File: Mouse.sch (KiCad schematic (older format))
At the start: 31 parts, among them J1 Conn_01x05_Male, U1 Left click, U2 Middle click, U3 Right Click, U4 LQ1, U5 Optical_Sensor

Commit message: Layout Updated
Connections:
- net Pin_2: no longer U1.2 (NO), U4.2
- net at LD2.1 (K): now also JP3.1; no longer R12.2
- net at LD2.2 (A): now also R12.2; no longer JP3.1
- net Pin_2J: now reaches C16.1, JP1.1, LD1.2 (A)
- net Pin_2J: now also U1.2 (NO), U4.2
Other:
- moved on the sheet: JP1, LD2, R12, U4
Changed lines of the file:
@@
 	4200 2650 4100 2650
 Text GLabel 2350 1550 0    50   Input ~ 0
-Pin_2
+Pin_2J
 Wire Wire Line
 	1300 4700 1100 4700
@@
 $EndComp
 $Comp
-L Device:C C8
-U 1 1 62FC41C4
-P 6300 2250
-F 0 "C8" V 6552 2250 50  0000 C CNN
-F 1 "C" V 6461 2250 50  0000 C CNN
-F 2 "Mouse:R_0603_1608_Logi" H 6338 2100 50  0001 C CNN
-F 3 "~" H 6300 2250 50  0001 C CNN
-	1    6300 2250
-	0    -1   -1   0
-$EndComp
-$Comp
 L power:GNDREF #PWR0109
 U 1 1 62FC9AD8
@@
 Wire Wire Line
 	6150 2250 5850 2250
-Text GLabel 6150 2400 0    50   Input ~ 0
-D-
 Wire Notes Line
 	550  7250 2850 7250
@@
 Text GLabel 5850 2250 0    50   Input ~ 0
 Pin_8
-Wire Wire Line
-	6200 2250 6200 2400
-Wire Wire Line
-	6200 2400 6150 2400
 Text GLabel 2700 3350 2    50   Input ~ 0
 Pin_7
@@
 Text GLabel 1550 6400 0    50   Input ~ 0
 Pin_3
-Text GLabel 850  6350 0    50   Input ~ 0
+Text GLabel 900  6350 0    50   Input ~ 0
 Pin_4
 $Comp
 L power:GNDREF #PWR0112
 U 1 1 62F9DBF5
-P 850 6550
-F 0 "#PWR0112" H 850 6300 50  0001 C CNN
-F 1 "GNDREF" V 855 6422 50  0000 R CNN
-F 2 "" H 850 6550 50  0001 C CNN
-F 3 "" H 850 6550 50  0001 C CNN
-	1    850  6550
-	1    0    0    -1
-$EndComp
-Text GLabel 850  6450 0    50   Input ~ 0
-Pin_2
+P 900 6550
+F 0 "#PWR0112" H 900 6300 50  0001 C CNN
+F 1 "GNDREF" V 905 6422 50  0000 R CNN
+F 2 "" H 900 6550 50  0001 C CNN
+F 3 "" H 900 6550 50  0001 C CNN
+	1    900  6550
+	1    0    0    -1
+$EndComp
+Text GLabel 900  6450 0    50   Input ~ 0
+Pin_2J
 $Comp
 L Optical_Mouse:LQ U4
 U 1 1 62F9C524
-P 1000 6350
-F 0 "U4" H 1078 6311 50  0000 L CNN
-F 1 "LQ1" H 1078 6220 50  0000 L CNN
-F 2 "Mouse:LQ1" H 1000 6450 50  0001 C CNN
-F 3 "" H 1000 6450 50  0001 C CNN
-	1    1000 6350
-	1    0    0    -1
-$EndComp
-Text GLabel 2550 6700 3    50   Input ~ 0
-Pin_2
+P 1050 6350
+F 0 "U4" H 1128 6311 50  0000 L CNN
+F 1 "LQ1" H 1128 6220 50  0000 L CNN
+F 2 "Mouse:LQ1" H 1050 6450 50  0001 C CNN
+F 3 "" H 1050 6450 50  0001 C CNN
+	1    1050 6350
+	1    0    0    -1
+$EndComp
 $Comp
 L LED:LD271 LD1
@@
 Wire Notes Line
 	550  4300 3250 4300
-Text GLabel 4950 1000 2    50   Input ~ 0
-Pin_1
 $Comp
 L Device:R R12
 U 1 1 62F83C24
-P 4200 1000
-F 0 "R12" V 3993 1000 50  0000 C CNN
-F 1 "330 LD2 resistor" V 4084 1000 50  0000 C CNN
-F 2 "Mouse:R_0603_1608_Logi" V 4130 1000 50  0001 C CNN
-F 3 "~" H 4200 1000 50  0001 C CNN
-	1    4200 1000
-	0    -1   -1   0
-$EndComp
-$Comp
-L LED:LD271 LD2
-U 1 1 62F8164E
-P 4550 1000
-F 0 "LD2" H 4500 1290 50  0000 C CNN
-F 1 "Sensor illumination" H 4500 1199 50  0000 C CNN
-F 2 "Mouse:LED_Sensor" H 4550 1175 50  0001 C CNN
-F 3 "http://www.alliedelec.com/m/d/40788c34903a719969df15f1fbea1056.pdf" H 4500 1000 50  0001 C CNN
-	1    4550 1000
-	1    0    0    -1
+P 3950 1000
+F 0 "R12" V 3743 1000 50  0000 C CNN
+F 1 "330 LD2 resistor" V 3834 1000 50  0000 C CNN
+F 2 "Mouse:R_0603_1608_Logi" V 3880 1000 50  0001 C CNN
+F 3 "~" H 3950 1000 50  0001 C CNN
+	1    3950 1000
+	0    -1   -1   0
 $EndComp
 Connection ~ 4200 2650
@@
 NoConn ~ 1000 2400
 $Comp
-L Device:R JP1
-U 1 1 63EBDACF
-P 2550 6550
-F 0 "JP1" H 2620 6596 50  0000 L CNN
-F 1 "R" H 2620 6505 50  0000 L CNN
-F 2 "Mouse:JP_Axial_DIN0207_L6.3mm_D2.5mm_P10.16mm_Horizontal" V 2480 6550 50  0001 C CNN
-F 3 "~" H 2550 6550 50  0001 C CNN
-	1    2550 6550
-	1    0    0    -1
-$EndComp
-$Comp
 L Device:R JP2
 U 1 1 63EBE5D2
@@
 	1    0    0    -1
 $EndComp
-Text GLabel 4050 1000 0    50   Input ~ 0
+Text GLabel 3800 1000 0    50   Input ~ 0
 Pin_5
+$Comp
+L power:GNDREF #PWR0104
+U 1 1 62FA90BC
+P 6400 1600
+F 0 "#PWR0104" H 6400 1350 50  0001 C CNN
+F 1 "GNDREF" H 6593 1457 50  0000 R CNN
+F 2 "" H 6400 1600 50  0001 C CNN
+F 3 "" H 6400 1600 50  0001 C CNN
+	1    6400 1600
+	1    0    0    -1
+$EndComp
+Wire Notes Line
+	6950 600  3450 600
+$Comp
+L Device:R R16
+U 1 1 62F9F594
+P 5850 1000
+F 0 "R16" V 6057 1000 50  0000 C CNN
+F 1 "R 000" V 5966 1000 50  0000 C CNN
+F 2 "Mouse:R_0603_1608_Logi" V 5780 1000 50  0001 C CNN
+F 3 "~" H 5850 1000 50  0001 C CNN
+	1    5850 1000
+	0    -1   -1   0
+$EndComp
+Connection ~ 6000 1000
+Wire Wire Line
+	5700 1000 5700 1150
+Wire Wire Line
+	1800 2400 1700 2400
+$Comp
+L Device:C C8
+U 1 1 62FC41C4
+P 6300 2250
+F 0 "C8" V 6552 2250 50  0000 C CNN
+F 1 "C" V 6461 2250 50  0000 C CNN
+F 2 "Mouse:R_0603_1608_Logi" H 6338 2100 50  0001 C CNN
+F 3 "~" H 6300 2250 50  0001 C CNN
+	1    6300 2250
+	0    -1   -1   0
+$EndComp
+Text GLabel 2600 6800 3    50   Input ~ 0
+Pin_2
+$Comp
+L Device:R JP1
+U 1 1 63EBDACF
+P 2600 6650
+F 0 "JP1" H 2670 6696 50  0000 L CNN
+F 1 "R" H 2670 6605 50  0000 L CNN
+F 2 "Mouse:JP_Axial_DIN0207_L6.3mm_D2.5mm_P10.16mm_Horizontal" V 2530 6650 50  0001 C CNN
+F 3 "~" H 2600 6650 50  0001 C CNN
+	1    2600 6650
+	1    0    0    -1
+$EndComp
+Wire Wire Line
+	6200 2250 6200 2400
+Wire Wire Line
+	6200 2400 6150 2400
+Text GLabel 6150 2400 0    50   Input ~ 0
+D-
 $Comp
 L Device:R JP3
@@
 $EndComp
 $Comp
-L power:GNDREF #PWR0104
-U 1 1 62FA90BC
-P 6400 1600
-F 0 "#PWR0104" H 6400 1350 50  0001 C CNN
-F 1 "GNDREF" H 6593 1457 50  0000 R CNN
-F 2 "" H 6400 1600 50  0001 C CNN
-F 3 "" H 6400 1600 50  0001 C CNN
-	1    6400 1600
-	1    0    0    -1
-$EndComp
-Wire Wire Line
-	2150 6400 2550 6400
+L LED:LD271 LD2
+U 1 1 62F8164E
+P 4450 1000
+F 0 "LD2" H 4400 1290 50  0000 C CNN
+F 1 "Sensor illumination" H 4400 1199 50  0000 C CNN
+F 2 "Mouse:LED_Sensor" H 4450 1175 50  0001 C CNN
+F 3 "http://www.alliedelec.com/m/d/40788c34903a719969df15f1fbea1056.pdf" H 4400 1000 50  0001 C CNN
+	1    4450 1000
+	-1   0    0    1
+$EndComp
+Text GLabel 4950 1000 2    50   Input ~ 0
+Pin_1
+Wire Wire Line
+	4350 1000 4100 1000
+Text GLabel 2600 6400 1    50   Input ~ 0
+Pin_2J
+Wire Wire Line
+	2150 6400 2600 6400
 Connection ~ 2150 6400
-Wire Notes Line
-	6950 600  3450 600
-$Comp
-L Device:R R16
-U 1 1 62F9F594
-P 5850 1000
-F 0 "R16" V 6057 1000 50  0000 C CNN
-F 1 "R 000" V 5966 1000 50  0000 C CNN
-F 2 "Mouse:R_0603_1608_Logi" V 5780 1000 50  0001 C CNN
-F 3 "~" H 5850 1000 50  0001 C CNN
-	1    5850 1000
-	0    -1   -1   0
-$EndComp
-Connection ~ 6000 1000
-Wire Wire Line
-	5700 1000 5700 1150
-Wire Wire Line
-	1800 2400 1700 2400
+Wire Wire Line
+	2600 6500 2600 6400
 $EndSCHEMATC

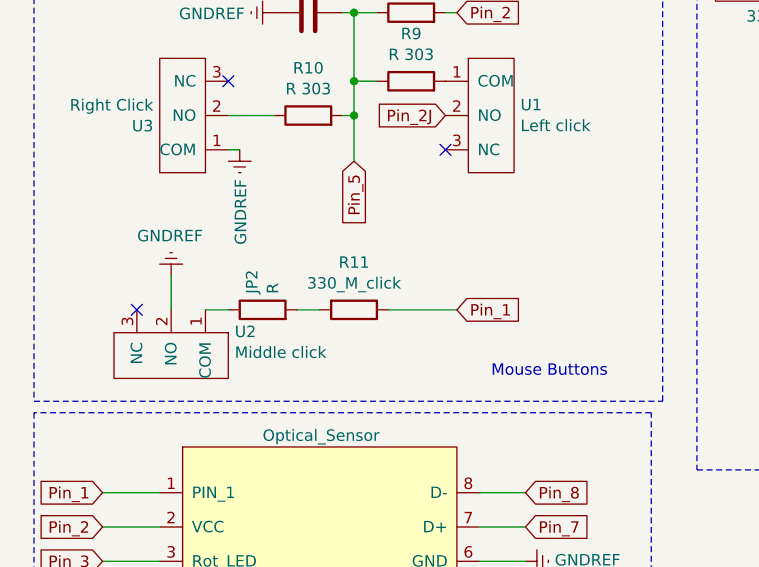
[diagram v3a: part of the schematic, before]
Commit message: Updated Schematics, Layout and Footprints
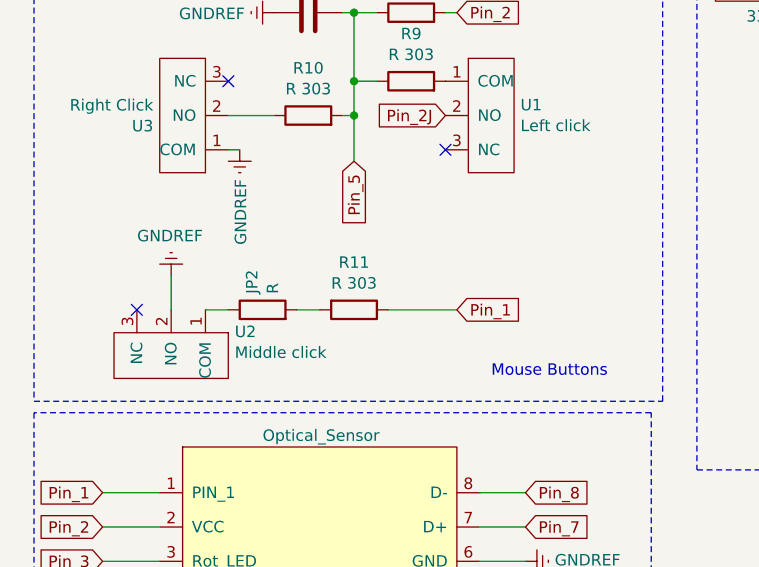
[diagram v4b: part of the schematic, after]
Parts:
- R11: value 330_M_click -> R 303
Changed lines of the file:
@@
 P 1950 2400
 F 0 "R11" V 1743 2400 50  0000 C CNN
-F 1 "330_M_click" V 1834 2400 50  0000 C CNN
+F 1 "R 303" V 1834 2400 50  0000 C CNN
 F 2 "Mouse:R_0603_1608_Logi" V 1880 2400 50  0001 C CNN
 F 3 "~" H 1950 2400 50  0001 C CNN

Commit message: Schematic Correction
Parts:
- C11, C13: value C -> C NC
- C12, C15: value C -> C 0.1uF
- C14: value C -> C 4.7uF
- C8, C9: value C -> C 0.01uF
- LQ1: renamed from U4; value LQ1 -> EL
- R12: value 330 LD2 resistor -> R 330
- R17: value R -> R NC
- renumbered U1 to SW1, U3 to SW2, U2 to SW3, U5 to U1
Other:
- moved on the sheet: C14, C15, JP4, R15, R16
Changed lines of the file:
@@
 $EndDescr
 $Comp
-L Optical_Mouse:switch U1
+L Optical_Mouse:switch SW1
 U 1 1 62F7695E
 P 2550 1550
-F 0 "U1" H 2678 1596 50  0000 L CNN
+F 0 "SW1" H 2678 1596 50  0000 L CNN
 F 1 "Left click" H 2678 1505 50  0000 L CNN
 F 2 "Mouse:SPDT_Switch" H 2800 1650 50  0001 C CNN
@@
 P 4350 2200
 F 0 "R17" V 4557 2200 50  0000 C CNN
-F 1 "R" V 4466 2200 50  0000 C CNN
+F 1 "R NC" V 4466 2200 50  0000 C CNN
 F 2 "Mouse:R_0603_1608_Logi" V 4280 2200 50  0001 C CNN
 F 3 "~" H 4350 2200 50  0001 C CNN
@@
 P 4650 2200
 F 0 "C13" V 4902 2200 50  0000 C CNN
-F 1 "C" V 4811 2200 50  0000 C CNN
+F 1 "C NC" V 4811 2200 50  0000 C CNN
 F 2 "Mouse:R_0603_1608_Logi" H 4688 2050 50  0001 C CNN
 F 3 "~" H 4650 2200 50  0001 C CNN
@@
 	1300 4600 1450 4600
 $Comp
-L Device:R R15
-U 1 1 62F9F9E0
-P 6150 1000
-F 0 "R15" V 6357 1000 50  0000 C CNN
-F 1 "R 1R0" V 6266 1000 50  0000 C CNN
-F 2 "Mouse:R_0603_1608_Logi" V 6080 1000 50  0001 C CNN
-F 3 "~" H 6150 1000 50  0001 C CNN
-	1    6150 1000
-	0    -1   -1   0
-$EndComp
-$Comp
 L Device:R R13
 U 1 1 62F9FE60
@@
 	0    -1   -1   0
 $EndComp
-$Comp
-L Device:C C14
-U 1 1 62FA0303
-P 6000 1450
-F 0 "C14" H 5885 1404 50  0000 R CNN
-F 1 "C" H 5885 1495 50  0000 R CNN
-F 2 "Mouse:R_0603_1608_Logi" H 6038 1300 50  0001 C CNN
-F 3 "~" H 6000 1450 50  0001 C CNN
-	1    6000 1450
-	-1   0    0    1
-$EndComp
-$Comp
-L Device:C C15
-U 1 1 62FA0A45
-P 6400 1450
-F 0 "C15" H 6515 1496 50  0000 L CNN
-F 1 "C" H 6515 1405 50  0000 L CNN
-F 2 "Mouse:R_0603_1608_Logi" H 6438 1300 50  0001 C CNN
-F 3 "~" H 6400 1450 50  0001 C CNN
-	1    6400 1450
-	1    0    0    -1
-$EndComp
-Text GLabel 5700 1450 3    50   Input ~ 0
-Pin_2
-Wire Wire Line
-	6000 1000 6000 1200
-Connection ~ 6000 1200
-Wire Wire Line
-	6000 1200 6000 1300
-Wire Wire Line
-	6400 1300 6400 1200
-Wire Wire Line
-	6000 1200 6400 1200
 Text GLabel 1100 4800 2    50   Input ~ 0
 VCC
@@
 Text GLabel 1300 5400 3    50   Input ~ 0
 D-
-Text GLabel 6450 1000 2    50   Input ~ 0
-VCC
-Wire Wire Line
-	6450 1000 6300 1000
-$Comp
-L power:GNDREF #PWR0103
-U 1 1 62FA8905
-P 6000 1600
-F 0 "#PWR0103" H 6000 1350 50  0001 C CNN
-F 1 "GNDREF" H 6199 1457 50  0000 R CNN
-F 2 "" H 6000 1600 50  0001 C CNN
-F 3 "" H 6000 1600 50  0001 C CNN
-	1    6000 1600
-	1    0    0    -1
-$EndComp
 Text GLabel 850  3650 0    50   Input ~ 0
 Pin_4
@@
 P 1750 1100
 F 0 "C11" V 2002 1100 50  0000 C CNN
-F 1 "C" V 1911 1100 50  0000 C CNN
+F 1 "C NC" V 1911 1100 50  0000 C CNN
 F 2 "Mouse:R_0603_1608_Logi" H 1788 950 50  0001 C CNN
 F 3 "~" H 1750 1100 50  0001 C CNN
@@
 P 4650 1650
 F 0 "C9" V 4902 1650 50  0000 C CNN
-F 1 "C" V 4811 1650 50  0000 C CNN
+F 1 "C  0.01uF" V 4811 1650 50  0000 C CNN
 F 2 "Mouse:R_0603_1608_Logi" H 4688 1500 50  0001 C CNN
 F 3 "~" H 4650 1650 50  0001 C CNN
@@
 	550  7250 2850 7250
 $Comp
-L Optical_Mouse:switch U3
+L Optical_Mouse:switch SW2
 U 1 1 62F77846
 P 1200 1550
-F 0 "U3" H 1328 1596 50  0000 L CNN
+F 0 "SW2" H 1328 1596 50  0000 L CNN
 F 1 "Right Click" H 1328 1505 50  0000 L CNN
 F 2 "Mouse:SPDT_Switch" H 1450 1650 50  0001 C CNN
@@
 $EndComp
 $Comp
-L Optical_Mouse:switch U2
+L Optical_Mouse:switch SW3
 U 1 1 62F76FC9
 P 1150 2600
-F 0 "U2" V 1046 2878 50  0000 L CNN
+F 0 "SW3" V 1046 2878 50  0000 L CNN
 F 1 "Middle click" V 1137 2878 50  0000 L CNN
 F 2 "Mouse:SPDT_Switch" H 1400 2700 50  0001 C CNN
@@
 Pin_2J
 $Comp
-L Optical_Mouse:LQ U4
+L Optical_Mouse:LQ LQ1
 U 1 1 62F9C524
 P 1050 6350
-F 0 "U4" H 1128 6311 50  0000 L CNN
-F 1 "LQ1" H 1128 6220 50  0000 L CNN
+F 0 "LQ1" H 1128 6311 50  0000 L CNN
+F 1 "EL" H 1128 6220 50  0000 L CNN
 F 2 "Mouse:LQ1" H 1050 6450 50  0001 C CNN
 F 3 "" H 1050 6450 50  0001 C CNN
@@
 P 3950 1000
 F 0 "R12" V 3743 1000 50  0000 C CNN
-F 1 "330 LD2 resistor" V 3834 1000 50  0000 C CNN
+F 1 "R 330 " V 3834 1000 50  0000 C CNN
 F 2 "Mouse:R_0603_1608_Logi" V 3880 1000 50  0001 C CNN
 F 3 "~" H 3950 1000 50  0001 C CNN
@@
 P 4650 2650
 F 0 "C12" V 4902 2650 50  0000 C CNN
-F 1 "C" V 4811 2650 50  0000 C CNN
+F 1 "C 0.1uF" V 4811 2650 50  0000 C CNN
 F 2 "Mouse:R_0603_1608_Logi" H 4688 2500 50  0001 C CNN
 F 3 "~" H 4650 2650 50  0001 C CNN
@@
 	2500 3650 2700 3650
 $Comp
-L Optical_Mouse:Optical_Sensor U5
+L Optical_Mouse:Optical_Sensor U1
 U 1 1 62F7519C
 P 1800 3450
-F 0 "U5" H 1750 3150 50  0000 L CNN
+F 0 "U1" H 1750 3150 50  0000 L CNN
 F 1 "Optical_Sensor" H 1550 3950 50  0000 L CNN
 F 2 "Mouse:Sensor" H 1800 3450 50  0001 C CNN
@@
 	0    -1   -1   0
 $EndComp
-$Comp
-L Device:R JP4
-U 1 1 63EBF40A
-P 5700 1300
-F 0 "JP4" H 5770 1346 50  0000 L CNN
-F 1 "R" H 5770 1255 50  0000 L CNN
-F 2 "Mouse:JP_Axial_DIN0207_L6.3mm_D2.5mm_P10.16mm_Horizontal" V 5630 1300 50  0001 C CNN
-F 3 "~" H 5700 1300 50  0001 C CNN
-	1    5700 1300
-	1    0    0    -1
-$EndComp
 Text GLabel 3800 1000 0    50   Input ~ 0
 Pin_5
-$Comp
-L power:GNDREF #PWR0104
-U 1 1 62FA90BC
-P 6400 1600
-F 0 "#PWR0104" H 6400 1350 50  0001 C CNN
-F 1 "GNDREF" H 6593 1457 50  0000 R CNN
-F 2 "" H 6400 1600 50  0001 C CNN
-F 3 "" H 6400 1600 50  0001 C CNN
-	1    6400 1600
-	1    0    0    -1
-$EndComp
-Wire Notes Line
-	6950 600  3450 600
-$Comp
-L Device:R R16
-U 1 1 62F9F594
-P 5850 1000
-F 0 "R16" V 6057 1000 50  0000 C CNN
-F 1 "R 000" V 5966 1000 50  0000 C CNN
-F 2 "Mouse:R_0603_1608_Logi" V 5780 1000 50  0001 C CNN
-F 3 "~" H 5850 1000 50  0001 C CNN
-	1    5850 1000
-	0    -1   -1   0
-$EndComp
-Connection ~ 6000 1000
-Wire Wire Line
-	5700 1000 5700 1150
 Wire Wire Line
 	1800 2400 1700 2400
@@
 P 6300 2250
 F 0 "C8" V 6552 2250 50  0000 C CNN
-F 1 "C" V 6461 2250 50  0000 C CNN
+F 1 "C 0.01uF" V 6461 2250 50  0000 C CNN
 F 2 "Mouse:R_0603_1608_Logi" H 6338 2100 50  0001 C CNN
 F 3 "~" H 6300 2250 50  0001 C CNN
@@
 Wire Wire Line
 	2600 6500 2600 6400
+Wire Wire Line
+	5750 950  5750 1150
+Wire Wire Line
+	5450 950  5450 1100
+Connection ~ 5750 950
+$Comp
+L Device:R R16
+U 1 1 62F9F594
+P 5600 950
+F 0 "R16" V 5807 950 50  0000 C CNN
+F 1 "R 000" V 5716 950 50  0000 C CNN
+F 2 "Mouse:R_0603_1608_Logi" V 5530 950 50  0001 C CNN
+F 3 "~" H 5600 950 50  0001 C CNN
+	1    5600 950
+	0    -1   -1   0
+$EndComp
+Wire Notes Line
+	6950 600  3450 600
+$Comp
+L power:GNDREF #PWR0104
+U 1 1 62FA90BC
+P 6350 1550
+F 0 "#PWR0104" H 6350 1300 50  0001 C CNN
+F 1 "GNDREF" H 6543 1407 50  0000 R CNN
+F 2 "" H 6350 1550 50  0001 C CNN
+F 3 "" H 6350 1550 50  0001 C CNN
+	1    6350 1550
+	1    0    0    -1
+$EndComp
+$Comp
+L Device:R JP4
+U 1 1 63EBF40A
+P 5450 1250
+F 0 "JP4" H 5520 1296 50  0000 L CNN
+F 1 "R" H 5520 1205 50  0000 L CNN
+F 2 "Mouse:JP_Axial_DIN0207_L6.3mm_D2.5mm_P10.16mm_Horizontal" V 5380 1250 50  0001 C CNN
+F 3 "~" H 5450 1250 50  0001 C CNN
+	1    5450 1250
+	1    0    0    -1
+$EndComp
+$Comp
+L power:GNDREF #PWR0103
+U 1 1 62FA8905
+P 5750 1550
+F 0 "#PWR0103" H 5750 1300 50  0001 C CNN
+F 1 "GNDREF" H 5949 1407 50  0000 R CNN
+F 2 "" H 5750 1550 50  0001 C CNN
+F 3 "" H 5750 1550 50  0001 C CNN
+	1    5750 1550
+	1    0    0    -1
+$EndComp
+Wire Wire Line
+	6200 950  6050 950
+Text GLabel 6200 950  2    50   Input ~ 0
+VCC
+Wire Wire Line
+	6350 1250 6350 1150
+Text GLabel 5450 1400 3    50   Input ~ 0
+Pin_2
+$Comp
+L Device:C C15
+U 1 1 62FA0A45
+P 6350 1400
+F 0 "C15" H 6465 1446 50  0000 L CNN
+F 1 "C 0.1uF" H 6465 1355 50  0000 L CNN
+F 2 "Mouse:R_0603_1608_Logi" H 6388 1250 50  0001 C CNN
+F 3 "~" H 6350 1400 50  0001 C CNN
+	1    6350 1400
+	1    0    0    -1
+$EndComp
+$Comp
+L Device:C C14
+U 1 1 62FA0303
+P 5750 1400
+F 0 "C14" H 5635 1354 50  0000 R CNN
+F 1 "C 4.7uF" H 5635 1445 50  0000 R CNN
+F 2 "Mouse:R_0603_1608_Logi" H 5788 1250 50  0001 C CNN
+F 3 "~" H 5750 1400 50  0001 C CNN
+	1    5750 1400
+	-1   0    0    1
+$EndComp
+$Comp
+L Device:R R15
+U 1 1 62F9F9E0
+P 5900 950
+F 0 "R15" V 6107 950 50  0000 C CNN
+F 1 "R 1R0" V 6016 950 50  0000 C CNN
+F 2 "Mouse:R_0603_1608_Logi" V 5830 950 50  0001 C CNN
+F 3 "~" H 5900 950 50  0001 C CNN
+	1    5900 950
+	0    -1   -1   0
+$EndComp
+Wire Wire Line
+	5750 1150 6350 1150
+Connection ~ 5750 1150
+Wire Wire Line
+	5750 1150 5750 1250
 $EndSCHEMATC
